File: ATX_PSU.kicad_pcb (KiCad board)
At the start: 4 copper layers, 100 x 100 mm, 194 parts, among them IC400 TLP185xSE, IC403 ACS71240, IC407 TLP185xSE, IC410 TLP185xSE, J200 09031967921, J400 XT60-Angled-F, J401 Conn_01x06_Pin, J800 USB_C_Receptacle_USB2.0_16P, Q400 AO3400A, Q401 HSBA8119, Q402 HSBA8119, Q403 HSBA8119, Q404 AO3400A, Q405 MMBT5551, Q700 MMST3904, U100 W25Q128, U301 TPS563201DDCR, U302 CH334P, U401 TPD2E2U06DCK, U402 TPD2E2U06DCK, U403 INA219AIDCNR, U404 ADS1115IDGS, U405 STM32H562VGTx, U500 TJA1044GTK_3Z, U600 TJA1044GTK_3Z, U700 STM32F103CBTx, U801 FSUSB42UMX, X300 Q13FC1350000400, Y400 ASE-xxxMHz, Y700 8 MHz, Y900 12Mhz

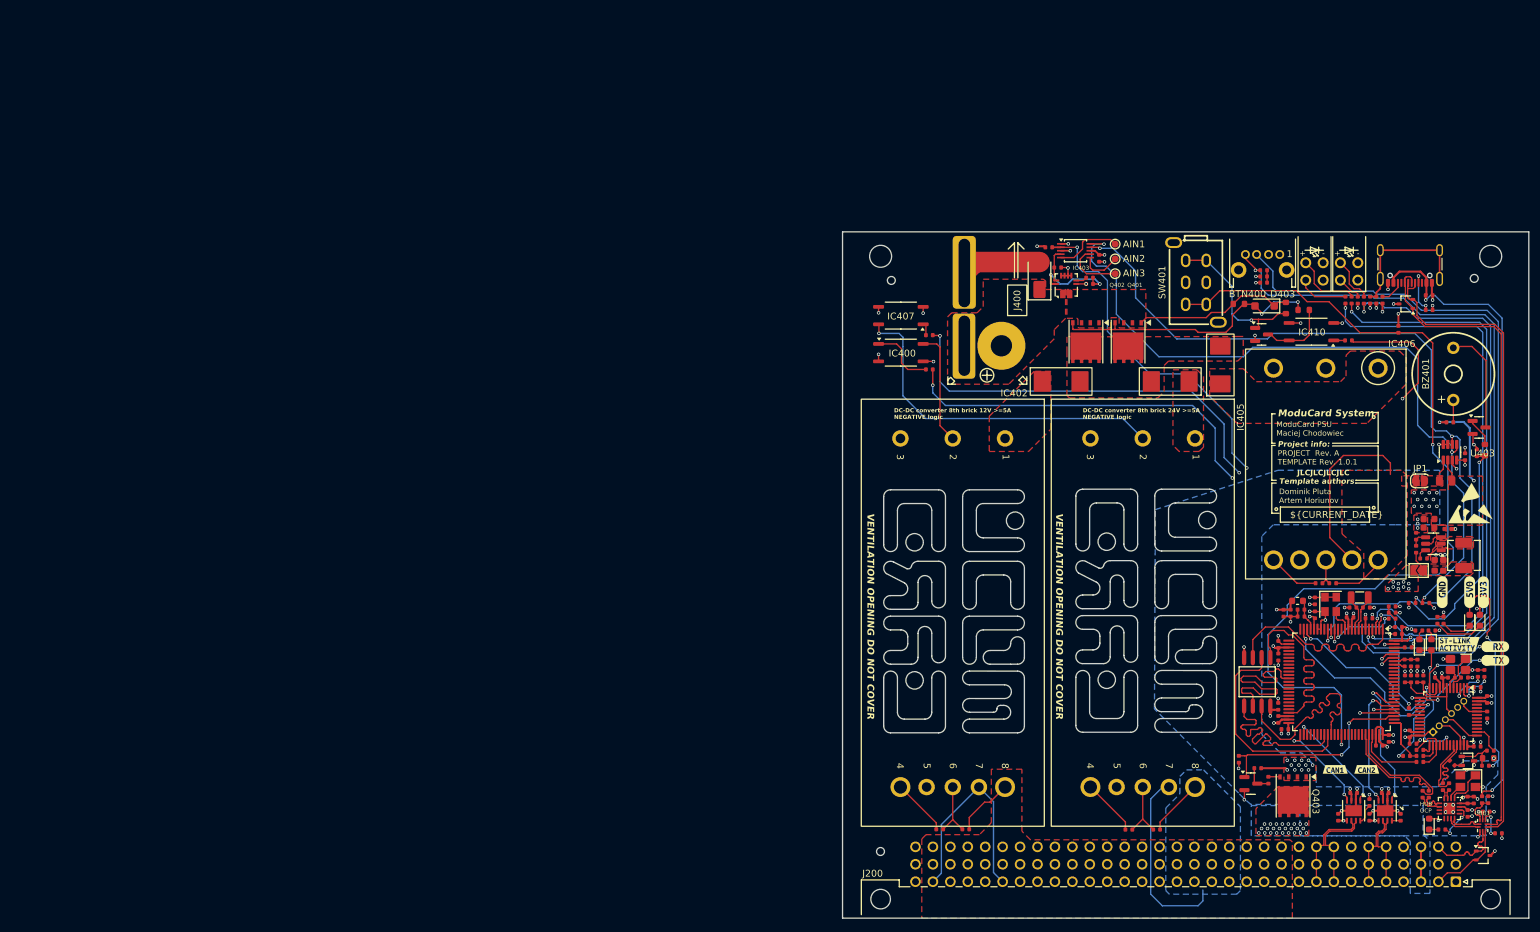
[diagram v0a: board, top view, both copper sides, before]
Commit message: fixed PS_ON# switching
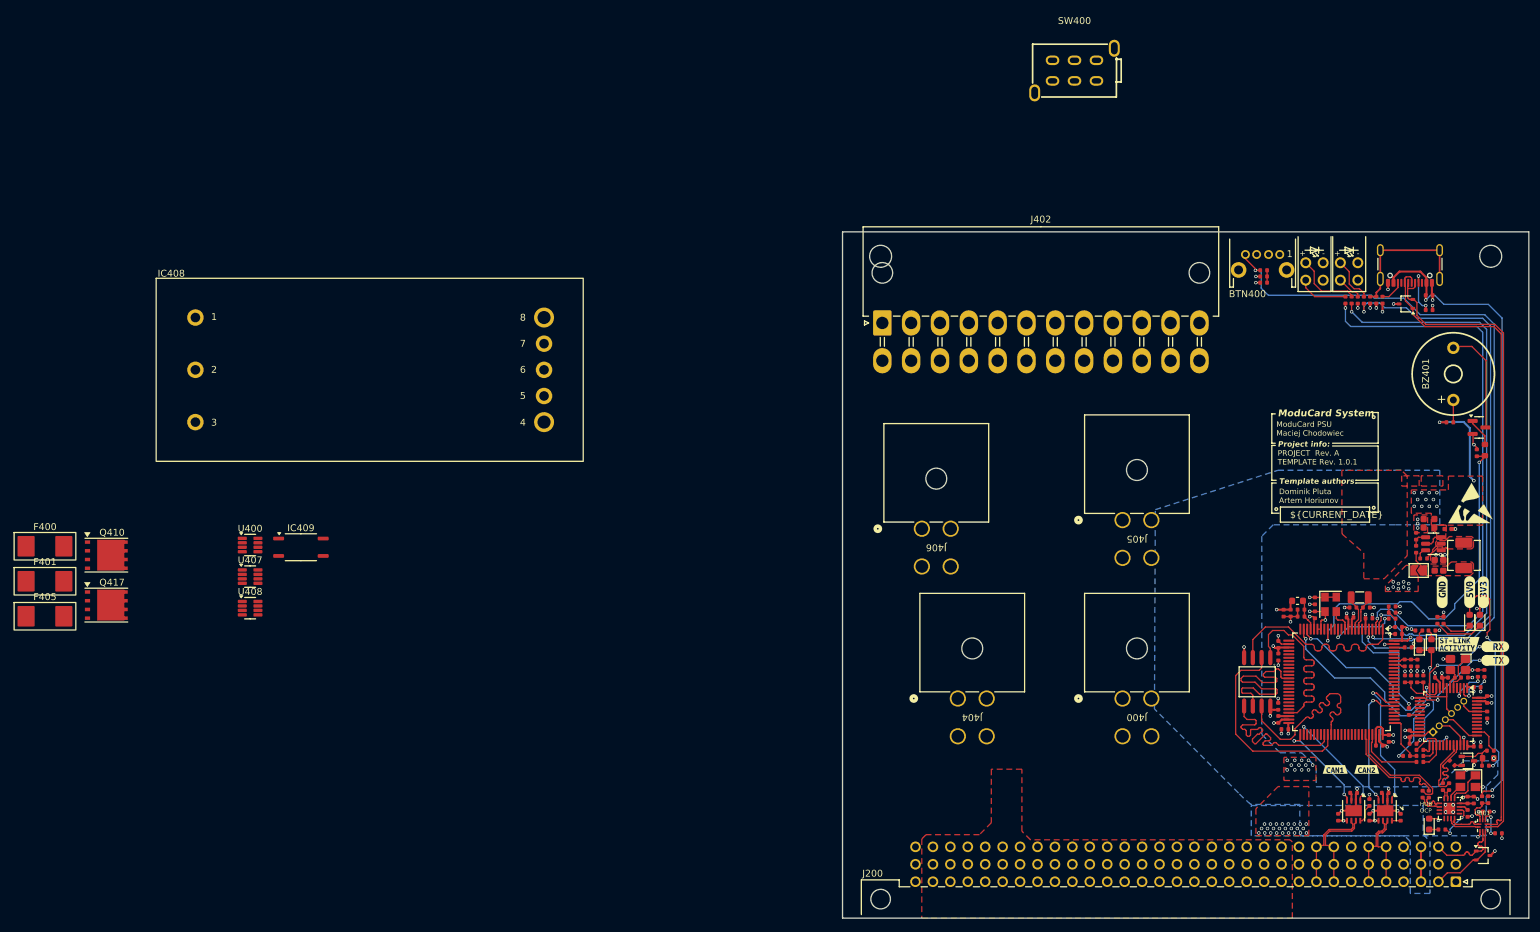
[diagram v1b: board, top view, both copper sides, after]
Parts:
- removed ? (x2): , 
- removed C418, C428, C430, C434: 100nF, PCM_JLCPCB:C_0402
- removed D403: 20V, Diode_SMD:D_SOD-123F
- removed D404: SMAJ64A, PCM_JLCPCB:D_SMA
- removed F402, F403, F404: 10A, FuseCustom:Fuse_2410_6125
- removed IC400, IC407, IC410: TLP185xSE, Package_SO:SOIC-4_4.55x3.7mm_P2.54mm
- removed IC402, IC405: ~, Brick_Converter:8th DC-DC converter
- removed IC403: ACS71240, Sensor_Current:Allegro_QFN-12-10-1EP_3x3mm_P0.5mm
- removed IC406: ~, Brick_Converter:16th DC-DC converter
- removed JP1: Solder Jumper, Jumper:SolderJumper-2_P1.3mm_Open_RoundedPad1.0x1.5mm
- removed Q400: AO3400A, PCM_JLCPCB:Q_SOT-23
- removed Q401, Q402, Q403: HSBA8119, DFN5060-8L:DFN5060-8L
- removed Q405: MMBT5551, PCM_JLCPCB:Q_SOT-23
- removed R400: 15kΩ, PCM_JLCPCB:R_0603
- removed R401, R410, R422, R423, R428, R429: 10kΩ, PCM_JLCPCB:R_0402
- removed R403: 100kΩ, PCM_JLCPCB:R_0603
- removed R413, R418: 1kΩ, PCM_JLCPCB:R_0402
- removed R414: 100kΩ, PCM_JLCPCB:R_0402
- removed R415: 5.1kΩ, PCM_JLCPCB:R_0603
- removed R417: 220Ω, PCM_JLCPCB:R_0402
- removed R419: 8mΩ, PCM_JLCPCB:R_0805
- removed R420, R421, R424, R425, R426, R427: R, PCM_JLCPCB:R_0402
- removed R430: 22Ω, PCM_JLCPCB:R_0402
- removed the REF** at (131.4, 58.1)
- removed the REF** at (122.0, 83.2)
- removed SW401: ~, PS-22F03:SW-TH_G-SWITCH-PS-22F03N
- removed TP400, TP401, TP402: TestPoint, TestPoint:TestPoint_Pad_D1.0mm
- removed U403: INA219AIDCNR, Package_TO_SOT_SMD:SOT-23-8
- removed U404: ADS1115IDGS, PCM_JLCPCB:TSSOP-10_3x3mm_P0.5mm
- added F400: 10A, FuseCustom:Fuse_2410_6125, F.Cu at (-76.8, 97.1)
- added F401: 10A, FuseCustom:Fuse_2410_6125, F.Cu at (-76.8, 102.2)
- added F405: 10A, FuseCustom:Fuse_2410_6125, F.Cu at (-76.8, 107.3)
- added IC408: ~, Brick_Converter:8th DC-DC converter, F.Cu at (-60.6, 58.1)
- added IC409: TLP185xSE, Package_SO:SOIC-4_4.55x3.7mm_P2.54mm, F.Cu at (-39.6, 97.2)
- added J402: ATX-24, Connector_Molex:Molex_Mini-Fit_Jr_5569-24A2_2x12_P4.20mm_Horizontal, F.Cu at (45.2, 64.6)
- added J404: 15246040, footprints:CONN_SDA-42404_04_MOL, F.Cu at (56.2, 119.3)
- added J405: 15246040, footprints:CONN_SDA-42404_04_MOL, F.Cu at (80.2, 93.3)
- added J406: 15246040, footprints:CONN_SDA-42404_04_MOL, F.Cu at (50.9, 94.5)
- added Q410: HSBA8119, DFN5060-8L:DFN5060-8L, F.Cu at (-67.9, 98.4)
- added Q417: HSBA8119, DFN5060-8L:DFN5060-8L, F.Cu at (-67.9, 105.7)
- added SW400: ~, PS-22F03:SW-TH_G-SWITCH-PS-22F03N, F.Cu at (73.2, 27.8)
- added U400: INA219AIDCNR, Package_TO_SOT_SMD:SOT-23-8, F.Cu at (-47.0, 96.9)
- added U407: INA219AIDCNR, Package_TO_SOT_SMD:SOT-23-8, F.Cu at (-47.0, 101.5)
- added U408: INA219AIDCNR, Package_TO_SOT_SMD:SOT-23-8, F.Cu at (-47.0, 106.1)
- J400: value XT60-Angled-F -> 15246040; footprint XT60-RightAngle:XT60-RightAngle-Adapter -> footprints:CONN_SDA-42404_04_MOL
- moved J400 61.0 mm to (80.2, 119.3), turned to 180 degrees
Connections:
- C309 pad 1: +5V -> +5V_SB
- C310 pad 1: +5V -> +5V_SB
- C311 pad 2: +5V -> +5V_SB
- C500 pad 2: +5V -> +5V_SB
- C600 pad 2: +5V -> +5V_SB
- C904 pad 1: +5V -> +5V_SB
- J200 pad a3: +5V_STDBY -> +5V
- J200 pad b3: +5V_STDBY -> +5V
- J200 pad c3: +5V_STDBY -> +5V
- J400 pad 1: Net-(IC403-IP+) -> GND
- U301 pad 3: +5V -> +5V_SB
- U301 pad 5: +5V -> +5V_SB
- U302 pad 15: +5V -> +5V_SB
- U405 pad 15: /Battery connector/MASTER_ON -> /MCU/MCU_ATX_ON
- U405 pad 16: /Battery connector/ADS115/RDY -> /ATX connector/PWR_OK
- U405 pad 78: /12V conveter + sensor/ON-OFF0 -> /MCU/ON-OFF0
- U405 pad 79: /12V conveter + sensor/ON-OFF1 -> /MCU/ON-OFF1
- U405 pad 80: /12V conveter + sensor/ON-OFF2 -> /MCU/ON-OFF2
- U405 pad 95: /5V converter + sensor/I2C.SCL -> /MCU/I2C1.SCL
- U405 pad 96: /5V converter + sensor/I2C.SDA -> /MCU/I2C1.SDA
- U500 pad 3: +5V -> +5V_SB
- U600 pad 3: +5V -> +5V_SB
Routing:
- net /MCU/Power_Button_IN: track 131.4 -> 0.00 mm, vias 2 -> 0
- net /5V converter + sensor/I2C.SCL: track 126.6 -> 0.00 mm, vias 4 -> 0
- net /5V converter + sensor/I2C.SDA: track 123.6 -> 0.00 mm, vias 4 -> 0
- net /12V conveter + sensor/ON-OFF2: track 105.6 -> 0.00 mm, vias 3 -> 0
- net /12V conveter + sensor/ON-OFF1: track 101.9 -> 0.00 mm, vias 3 -> 0
- net /MCU/SWD.~{RST}: track 127.9 -> 26.9 mm
- net /Battery connector/ADS115/RDY: track 82.9 -> 0.00 mm, vias 3 -> 0
- net /Battery connector/MASTER_ON: track 61.1 -> 0.00 mm, vias 2 -> 0
- net GND: track 147.4 -> 88.5 mm, vias 90 -> 73
- net /??V converter + sensor/ON/OFF: track 51.1 -> 0.00 mm, vias 1 -> 0
- net +12V: track 40.6 -> 0.00 mm
- net Net-(D403-A): track 40.1 -> 0.00 mm, vias 2 -> 0
- net +24V: track 34.8 -> 0.00 mm
- net /5V converter + sensor/PreJumper: track 34.2 -> 0.00 mm
- net /12V conveter + sensor/ON-OFF0: track 30.2 -> 0.00 mm, vias 2 -> 0
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- added copper zone on F.Cu, net (none)
- removed copper zone on B.Cu, net +24V
- removed copper zone on B.Cu, net +5V_STDBY
- removed copper zone on F.Cu, net +5V_STDBY
- removed copper zone on F.Cu, net /12V conveter + sensor/BATTERY
- removed copper zone on F.Cu, net /12V conveter + sensor/FUSE
- removed copper zone on F.Cu, net /5V converter + sensor/BATTERY_FUSED
- removed copper zone on F.Cu, net /5V converter + sensor/PawełJumper
- removed copper zone on F.Cu, net /5V converter + sensor/PreJumper
- removed copper zone on F.Cu, net /??V converter + sensor/FUSE
- removed copper zone on F.Cu, net Net-(D403-K)
- removed copper zone on F.Cu, net Net-(IC403-IP+)
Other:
- outline, holes or cut-outs redrawn
- board text removed: "12V"
- board text removed: "5v"
- board text removed: "65V in"
- board text removed: "AIN1"
- board text removed: "AIN2"
- board text removed: "AIN3"
- board text removed: "ARB V"
- board text removed: "DC-DC converter 8th brick 12V >=5A NEGATIVE logic"
- board text removed: "DC-DC converter 8th brick 24V >=5A NEGATIVE logic"
- board text removed: "INFO:"
- board text removed: "VENTILATION OPENING DO NOT COVER"

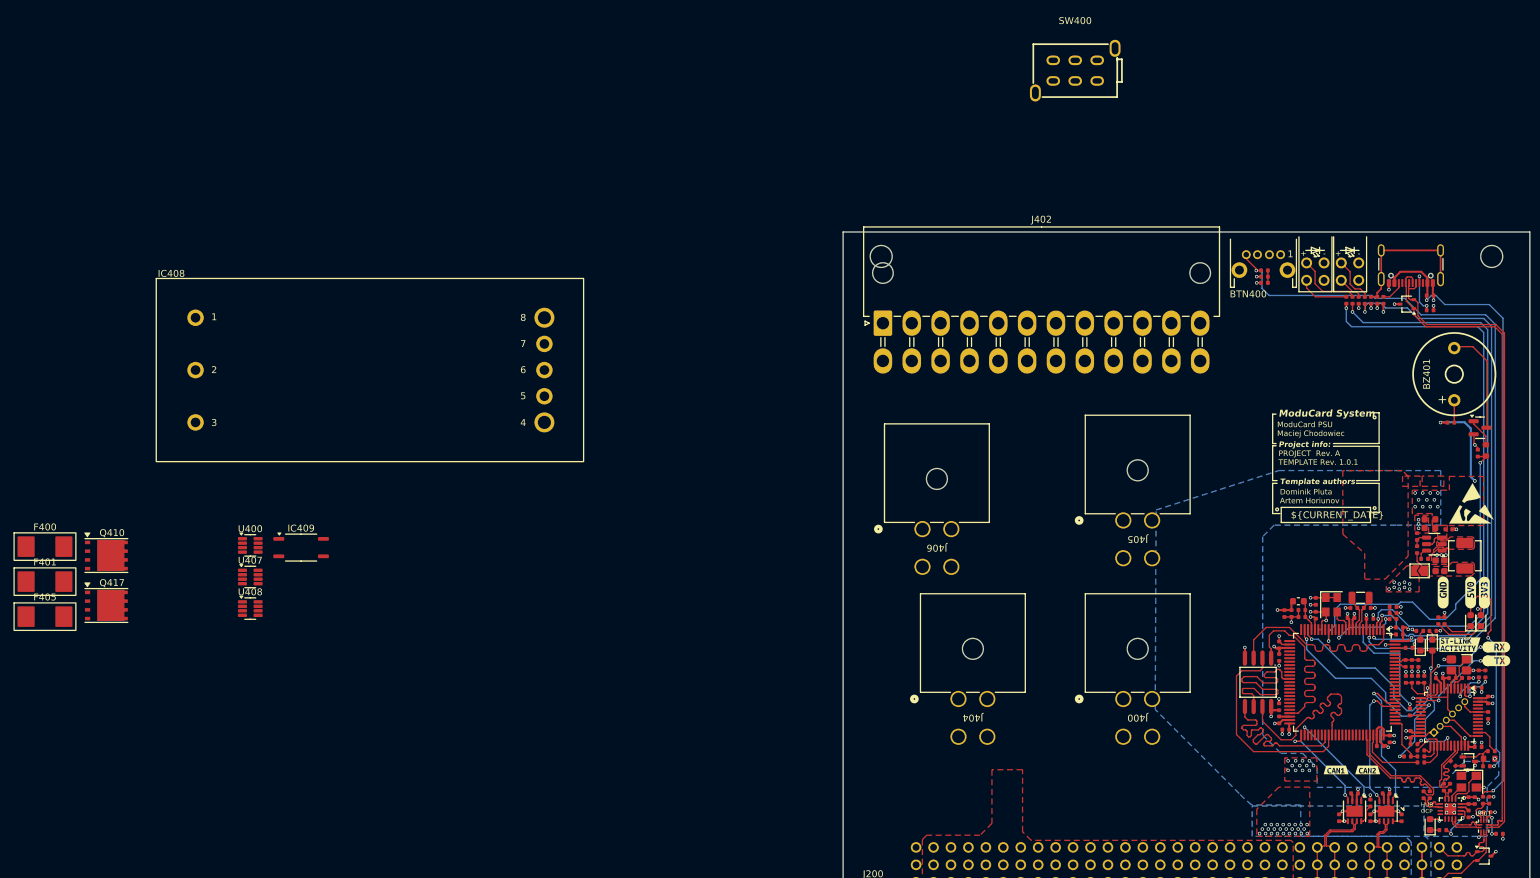
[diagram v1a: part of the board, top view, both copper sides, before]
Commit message: removed III out of IV 4 pin connector
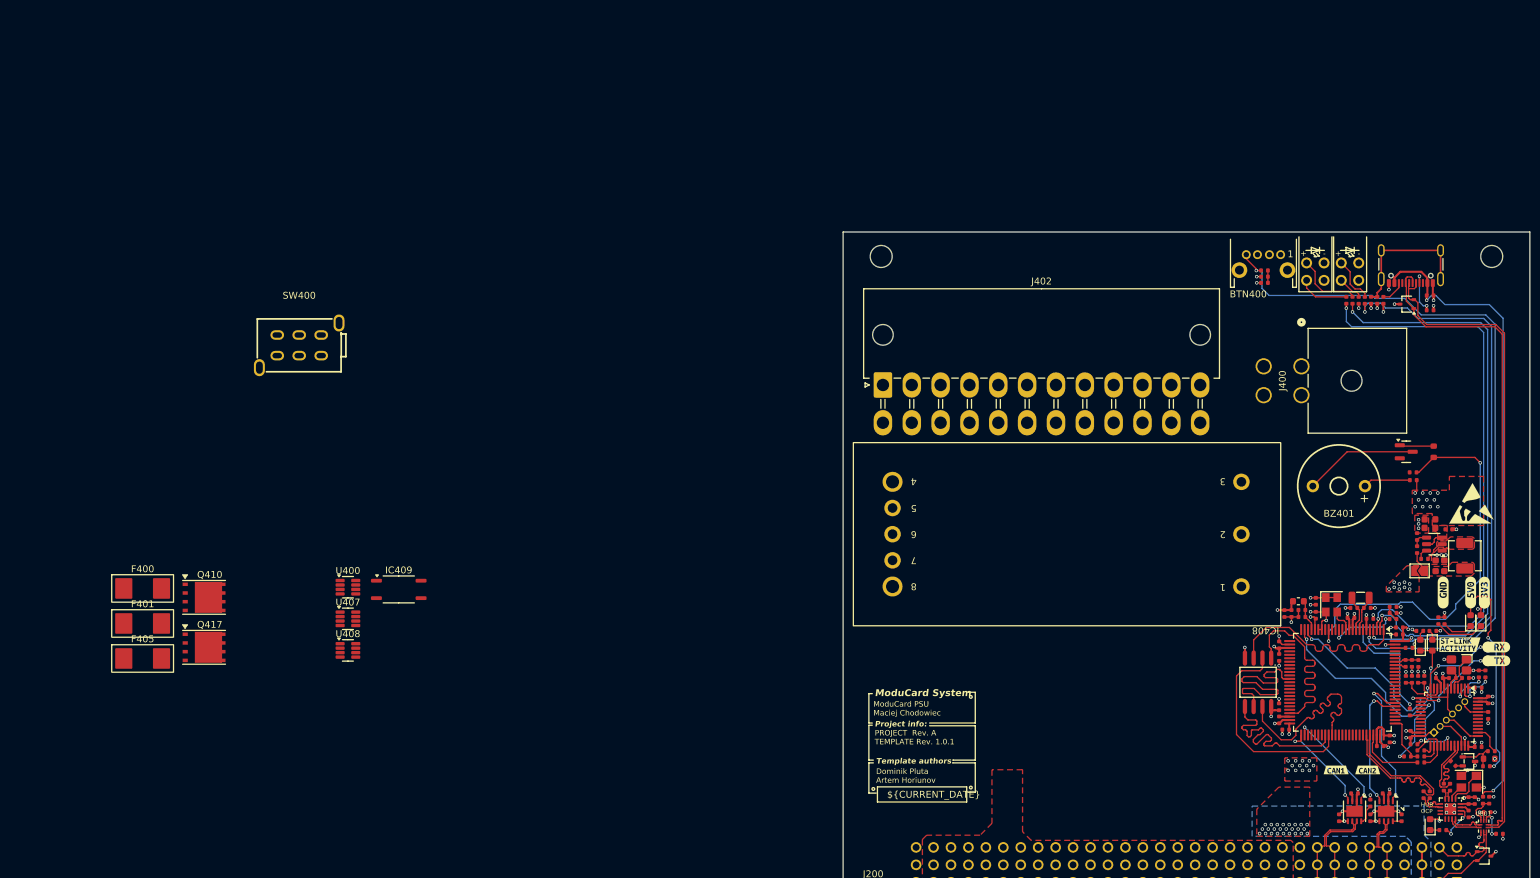
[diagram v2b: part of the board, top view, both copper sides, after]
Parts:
- removed J404, J405, J406: 15246040, footprints:CONN_SDA-42404_04_MOL
- moved IC408 171.4 mm to (103.1, 108.6), turned to 180 degrees
- moved SW400 119.9 mm to (-39.8, 67.8)
- moved J400 54.9 mm to (106.1, 70.8), turned to 90 degrees
- moved BZ401 23.4 mm to (111.6, 88.3), turned to 180 degrees
- moved Q410 15.5 mm to (-53.7, 104.5)
- moved Q417 15.5 mm to (-53.7, 111.8)
- moved U400 15.5 mm to (-32.7, 103.0)
- moved U407 15.5 mm to (-32.7, 107.6)
- moved U408 15.5 mm to (-32.7, 112.2)
- moved F400 15.5 mm to (-62.6, 103.2)
- moved F405 15.5 mm to (-62.6, 113.4)
- moved IC409 15.5 mm to (-25.3, 103.3)
- moved F401 15.5 mm to (-62.6, 108.3)
- moved Q404 11.3 mm to (121.4, 83.3)
- moved R445 10.0 mm to (122.4, 87.4), turned to 180 degrees
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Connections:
- SW400 pad 2: +5V_SB -> GND
- SW400 pad 3: unconnected-(SW400-NC-Pad3) -> GND
- SW400 pad 5: +5V_SB -> GND
- SW400 pad 6: unconnected-(SW400-NC-Pad6) -> GND
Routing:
- net +5V: track 52.0 -> 40.2 mm, vias 53 -> 51
- net /MCU/Buzzer: track 51.7 -> 59.6 mm
- net Net-(BZ401-+): track 3.45 -> 6.89 mm
- net GND: track 88.5 -> 86.0 mm, vias 73 -> 72
- net Net-(BZ401--): track 15.3 -> 16.6 mm
- net Net-(Q404-G): track 4.17 -> 4.99 mm
- removed copper zone on F.Cu, net (none)
